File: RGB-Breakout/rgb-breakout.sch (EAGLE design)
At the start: 2 parts

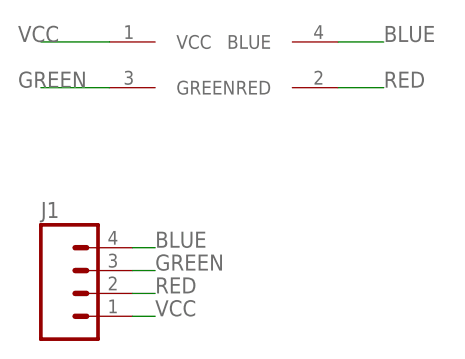
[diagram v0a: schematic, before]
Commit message: new breakout
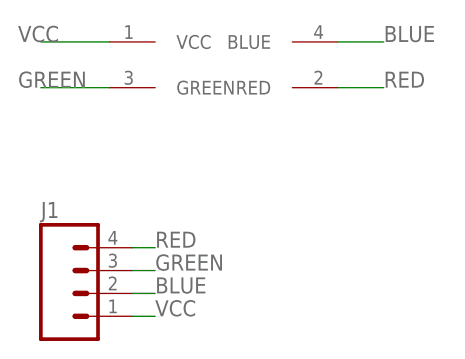
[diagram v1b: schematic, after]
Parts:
- U$1: value XZCMEDGCBD110W-RGBXZCMEDGCBD110W-RGB -> XZCMEDGCBD110W-RGB; device leds:XZCMEDGCBD110W-RGBXZCMEDGCBD110W-RGB -> leds:XZCMEDGCBD110W-RGB
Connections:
- net BLUE: now also J1.2; no longer J1.4
- net RED: now also J1.4; no longer J1.2
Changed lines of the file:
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@@
 </classes>
 <parts>
-<part name="U$1" library="leds" deviceset="XZCMEDGCBD110W-RGB" device="XZCMEDGCBD110W-RGB" package3d_urn="urn:adsk.eagle:package:19572740/1"/>
+<part name="U$1" library="leds" deviceset="XZCMEDGCBD110W-RGB" device=""/>
 <part name="J1" library="connector" deviceset="M04" device="LONGPADS"/>
 </parts>
@@
 </segment>
 <segment>
-<pinref part="J1" gate="G$1" pin="4"/>
-<wire x1="20.32" y1="53.34" x2="22.86" y2="53.34" width="0.1524" layer="91"/>
-<label x="22.86" y="53.34" size="1.778" layer="95"/>
+<pinref part="J1" gate="G$1" pin="2"/>
+<wire x1="20.32" y1="48.26" x2="22.86" y2="48.26" width="0.1524" layer="91"/>
+<label x="22.86" y="48.26" size="1.778" layer="95"/>
 </segment>
 </net>
@@
 </segment>
 <segment>
-<pinref part="J1" gate="G$1" pin="2"/>
-<wire x1="20.32" y1="48.26" x2="22.86" y2="48.26" width="0.1524" layer="91"/>
-<label x="22.86" y="48.26" size="1.778" layer="95"/>
+<pinref part="J1" gate="G$1" pin="4"/>
+<wire x1="20.32" y1="53.34" x2="22.86" y2="53.34" width="0.1524" layer="91"/>
+<label x="22.86" y="53.34" size="1.778" layer="95"/>
 </segment>
 </net>
@@
 </schematic>
 </drawing>
-<compatibility>
-<note version="8.3" severity="warning">
-Since Version 8.3, EAGLE supports URNs for individual library
-assets (packages, symbols, and devices). The URNs of those assets
-will not be understood (or retained) with this version.
-</note>
-<note version="8.3" severity="warning">
-Since Version 8.3, EAGLE supports the association of 3D packages
-with devices in libraries, schematics, and board files. Those 3D
-packages will not be understood (or retained) with this version.
-</note>
-</compatibility>
 </eagle>
